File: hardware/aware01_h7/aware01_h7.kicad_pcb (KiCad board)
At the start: 4 copper layers, 76.7 x 110 mm, 138 parts, among them IC2 TLV320AIC3204IRHBR, J1 Conn_01x06_Pin, J10 CV1_IN, J11 InL, J13 OutR, J2 Conn_01x03_Pin, J3 Conn_02x05_Odd_Even, J4 InR, J5 GATE1_IN, J6 OutL, J7 GATE2_IN, J8 CV2_IN, J9 V/OCT_IN, Q1 MMBT3904, Q2 MMBT3904, SW1 SW_Push, SW2 SW_Push, SW3 SW_Push, U1 STM32H7B0ZBTx, U10 NE5532DRG4, U11 LMV722IDR, U13 LMV722IDR, U2 IS45S16800F-7TLA2, U3 10k, U4 10k, U5 10k, U6 10k, U7 LM1117MP-3.3, U8 LM4040DBZ-10, U9 NE5532DRG4, Y1 WE-XTAL 24.0MHz 50ppm

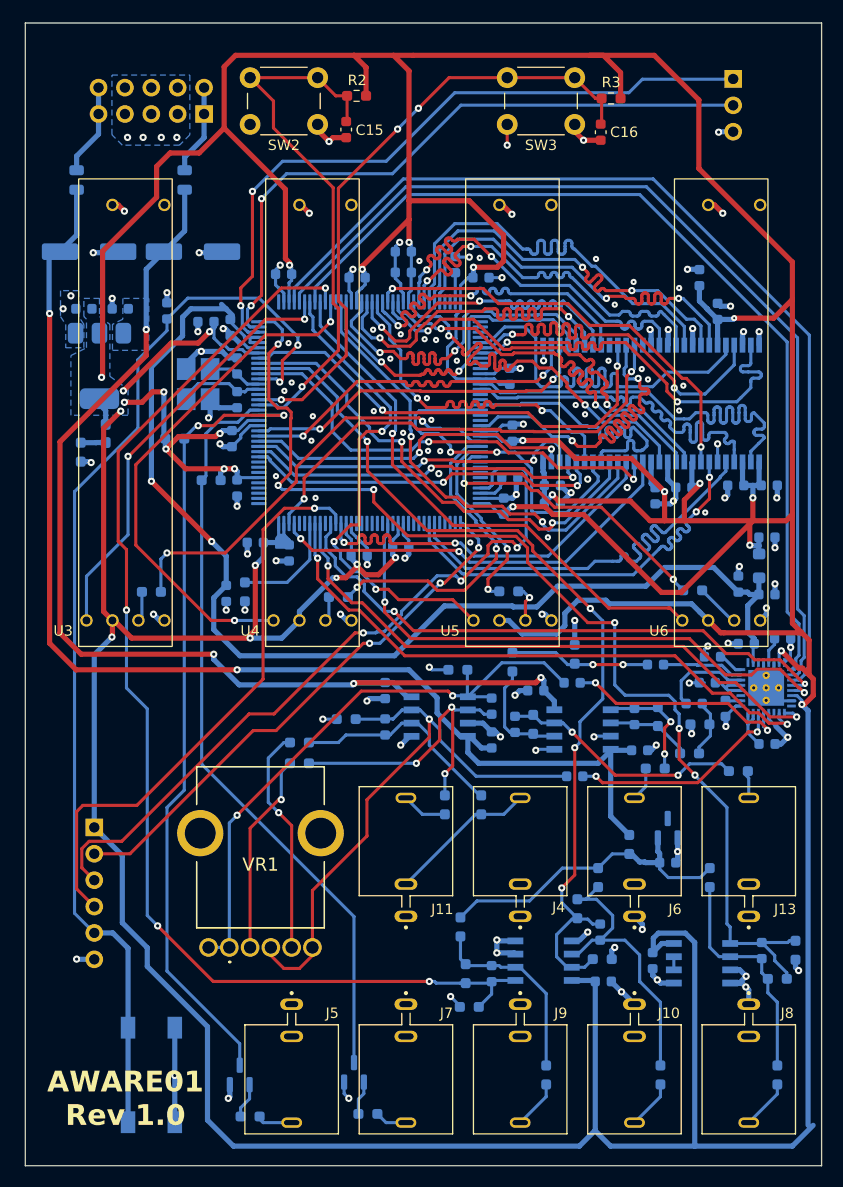
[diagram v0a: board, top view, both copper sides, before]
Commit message: add series termination resistors
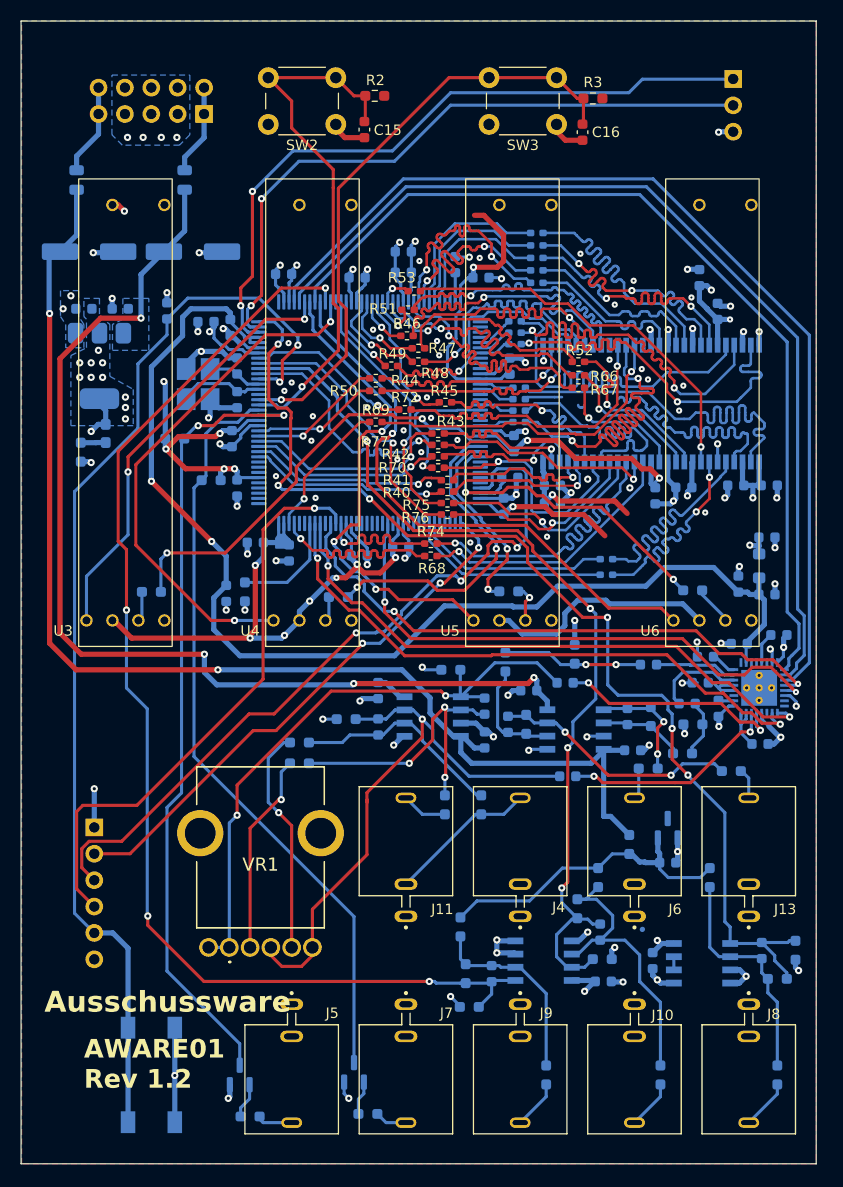
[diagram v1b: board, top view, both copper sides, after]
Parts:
- added R40: 10, Resistor_SMD:R_0402_1005Metric_Pad0.72x0.64mm_HandSolder, F.Cu at (201.5, 80.6)
- added R41: 10, Resistor_SMD:R_0402_1005Metric_Pad0.72x0.64mm_HandSolder, F.Cu at (201.5, 79.5)
- added R42: 10, Resistor_SMD:R_0402_1005Metric_Pad0.72x0.64mm_HandSolder, F.Cu at (200.6, 77.2)
- added R43: 10, Resistor_SMD:R_0402_1005Metric_Pad0.72x0.64mm_HandSolder, F.Cu at (200.6, 75.0)
- added R44: 10, Resistor_SMD:R_0402_1005Metric_Pad0.72x0.64mm_HandSolder, F.Cu at (194.6, 69.7)
- added R45: 10, Resistor_SMD:R_0402_1005Metric_Pad0.72x0.64mm_HandSolder, F.Cu at (201.3, 72.0)
- added R46: 10, Resistor_SMD:R_0402_1005Metric_Pad0.72x0.64mm_HandSolder, F.Cu at (197.6, 65.6)
- added R47: 10, Resistor_SMD:R_0402_1005Metric_Pad0.72x0.64mm_HandSolder, F.Cu at (198.7, 66.8)
- added R48: 10, Resistor_SMD:R_0402_1005Metric_Pad0.72x0.64mm_HandSolder, F.Cu at (198.7, 68.1)
- added R49: 10, Resistor_SMD:R_0402_1005Metric_Pad0.72x0.64mm_HandSolder, F.Cu at (196.1, 68.5)
- added R50: 10, Resistor_SMD:R_0402_1005Metric_Pad0.72x0.64mm_HandSolder, F.Cu at (194.6, 70.9)
- added R51: 10, Resistor_SMD:R_0402_1005Metric_Pad0.72x0.64mm_HandSolder, F.Cu at (197.7, 63.1)
- added R52: 10, Resistor_SMD:R_0402_1005Metric_Pad0.72x0.64mm_HandSolder, F.Cu at (214.1, 68.1)
- added R53: 10, Resistor_SMD:R_0402_1005Metric_Pad0.72x0.64mm_HandSolder, F.Cu at (198.3, 61.3)
- added R54: 10, Resistor_SMD:R_0402_1005Metric_Pad0.72x0.64mm_HandSolder, B.Cu at (216.8, 88.6)
- added R55: 10, Resistor_SMD:R_0402_1005Metric_Pad0.72x0.64mm_HandSolder, B.Cu at (216.8, 87.1)
- added R56: 10, Resistor_SMD:R_0402_1005Metric_Pad0.72x0.64mm_HandSolder, B.Cu at (208.4, 71.7)
- added R57: 10, Resistor_SMD:R_0402_1005Metric_Pad0.72x0.64mm_HandSolder, B.Cu at (208.4, 70.6)
- added R58: 10, Resistor_SMD:R_0402_1005Metric_Pad0.72x0.64mm_HandSolder, B.Cu at (210.1, 60.5)
- added R59: 10, Resistor_SMD:R_0402_1005Metric_Pad0.72x0.64mm_HandSolder, B.Cu at (210.1, 59.3)
- added R60: 10, Resistor_SMD:R_0402_1005Metric_Pad0.72x0.64mm_HandSolder, B.Cu at (210.1, 55.7)
- added R61: 10, Resistor_SMD:R_0402_1005Metric_Pad0.72x0.64mm_HandSolder, B.Cu at (210.1, 56.9)
- added R62: 10, Resistor_SMD:R_0402_1005Metric_Pad0.72x0.64mm_HandSolder, B.Cu at (210.1, 58.1)
- added R63: 10, Resistor_SMD:R_0402_1005Metric_Pad0.72x0.64mm_HandSolder, B.Cu at (208.0, 64.2)
- added R64: 10, Resistor_SMD:R_0402_1005Metric_Pad0.72x0.64mm_HandSolder, B.Cu at (208.0, 65.3)
- added R65: 10, Resistor_SMD:R_0402_1005Metric_Pad0.72x0.64mm_HandSolder, B.Cu at (208.0, 66.4)
- added R66: 10, Resistor_SMD:R_0402_1005Metric_Pad0.72x0.64mm_HandSolder, F.Cu at (214.1, 69.4)
- added R67: 10, Resistor_SMD:R_0402_1005Metric_Pad0.72x0.64mm_HandSolder, F.Cu at (214.1, 70.6)
- added R68: 10, Resistor_SMD:R_0402_1005Metric_Pad0.72x0.64mm_HandSolder, F.Cu at (199.9, 86.8)
- added R69: 10, Resistor_SMD:R_0402_1005Metric_Pad0.72x0.64mm_HandSolder, F.Cu at (194.6, 73.9)
- added R70: 10, Resistor_SMD:R_0402_1005Metric_Pad0.72x0.64mm_HandSolder, F.Cu at (200.6, 78.3)
- added R71: 10, Resistor_SMD:R_0402_1005Metric_Pad0.72x0.64mm_HandSolder, B.Cu at (208.4, 72.8)
- added R72: 10, Resistor_SMD:R_0402_1005Metric_Pad0.72x0.64mm_HandSolder, F.Cu at (197.4, 72.7)
- added R73: 10, Resistor_SMD:R_0402_1005Metric_Pad0.72x0.64mm_HandSolder, B.Cu at (208.4, 73.9)
- added R74: 10, Resistor_SMD:R_0402_1005Metric_Pad0.72x0.64mm_HandSolder, F.Cu at (199.9, 85.6)
- added R75: 10, Resistor_SMD:R_0402_1005Metric_Pad0.72x0.64mm_HandSolder, F.Cu at (201.5, 81.7)
- added R76: 10, Resistor_SMD:R_0402_1005Metric_Pad0.72x0.64mm_HandSolder, F.Cu at (201.5, 82.8)
- added R77: 10, Resistor_SMD:R_0402_1005Metric_Pad0.72x0.64mm_HandSolder, F.Cu at (200.6, 76.1)
- U8: value LM4040DBZ-10 -> LM4040DIM3X-10
- moved C15 1.75 mm to (193.5, 45.8)
- moved C16 1.75 mm to (214.5, 46.0)
- moved R2 1.75 mm to (194.5, 42.5)
- moved R3 1.75 mm to (215.5, 42.8)
- moved SW2 1.75 mm to (190.8, 45.2)
- moved SW3 1.75 mm to (212.0, 45.2)
- moved C27 1.01 mm to (207.9, 76.0)
- moved C29 0.97 mm to (207.5, 68.5)
- moved U6 0.85 mm to (227.0, 93.0)
- moved C39 0.68 mm to (231.6, 104.9)
- moved C40 0.68 mm to (226.3, 96.5)
- moved C41 0.68 mm to (227.6, 101.5)
- moved C42 0.68 mm to (225.8, 99.0)
- moved C43 0.68 mm to (194.8, 99.8)
- moved C44 0.68 mm to (205.1, 104.5)
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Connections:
- U2 pad 10: /FMC_D5 -> Net-(U2-DQ5)
- U2 pad 11: /FMC_D6 -> Net-(U2-DQ6)
- U2 pad 13: /FMC_D7 -> Net-(U2-DQ7)
- U2 pad 15: /FMC_NBL0 -> Net-(U2-DQML)
- U2 pad 16: /FMC_SDNWE -> Net-(U2-~{WE})
- U2 pad 17: /FMC_SDNCAS -> Net-(U2-~{CAS})
- U2 pad 18: /FMC_SDNRAS -> Net-(U2-~{RAS})
- U2 pad 19: /FMC_SDNE0 -> Net-(U2-~{CS})
- U2 pad 2: /FMC_D0 -> Net-(U2-DQ0)
- U2 pad 20: /FMC_BA0 -> Net-(U2-BA0)
- U2 pad 21: /FMC_BA1 -> Net-(U2-BA1)
- U2 pad 22: /FMC_A10 -> Net-(U2-A10)
- U2 pad 23: /FMC_A0 -> Net-(U2-A0)
- U2 pad 24: /FMC_A1 -> Net-(U2-A1)
- U2 pad 25: /FMC_A2 -> Net-(U2-A2)
- U2 pad 26: /FMC_A3 -> Net-(U2-A3)
- U2 pad 29: /FMC_A4 -> Net-(U2-A4)
- U2 pad 30: /FMC_A5 -> Net-(U2-A5)
- U2 pad 31: /FMC_A6 -> Net-(U2-A6)
- U2 pad 32: /FMC_A7 -> Net-(U2-A7)
- U2 pad 33: /FMC_A8 -> Net-(U2-A8)
- U2 pad 34: /FMC_A9 -> Net-(U2-A9)
- U2 pad 35: /FMC_A11 -> Net-(U2-A11)
- U2 pad 37: /FMC_SDCKE0 -> Net-(U2-CKE)
- U2 pad 38: /FMC_SDCLK -> Net-(U2-CLK)
- U2 pad 39: /FMC_NBL1 -> Net-(U2-DQMH)
- U2 pad 4: /FMC_D1 -> Net-(U2-DQ1)
- U2 pad 42: /FMC_D8 -> Net-(U2-DQ8)
- U2 pad 44: /FMC_D9 -> Net-(U2-DQ9)
- U2 pad 45: /FMC_D10 -> Net-(U2-DQ10)
- U2 pad 47: /FMC_D11 -> Net-(U2-DQ11)
- U2 pad 48: /FMC_D12 -> Net-(U2-DQ12)
- U2 pad 5: /FMC_D2 -> Net-(U2-DQ2)
- U2 pad 50: /FMC_D13 -> Net-(U2-DQ13)
- U2 pad 51: /FMC_D14 -> Net-(U2-DQ14)
- U2 pad 53: /FMC_D15 -> Net-(U2-DQ15)
- U2 pad 7: /FMC_D3 -> Net-(U2-DQ3)
- U2 pad 8: /FMC_D4 -> Net-(U2-DQ4)
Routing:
- net +3.3V: track 742.1 -> 246.5 mm, vias 30 -> 42
- net /FMC_D0: track 44.8 -> 3.29 mm
- net /FMC_D13: track 44.8 -> 3.66 mm
- net Net-(U2-CLK): track 0.00 -> 40.3 mm, vias 0 -> 2
- net Net-(U2-DQ13): track 0.00 -> 40.2 mm
- net Net-(U2-DQ0): track 0.00 -> 40.0 mm
- net /FMC_D4: track 42.0 -> 3.08 mm, vias 2 -> 1
- net Net-(U2-DQ4): track 0.00 -> 37.9 mm, vias 0 -> 1
- net Net-(U2-DQ15): track 0.00 -> 37.6 mm, vias 0 -> 2
- net Net-(U2-DQ14): track 0.00 -> 37.0 mm, vias 0 -> 2
- net /FMC_D15: track 39.9 -> 3.09 mm, vias 2 -> 0
- net /FMC_D14: track 40.1 -> 3.34 mm, vias 2 -> 0
- net /FMC_D1: track 37.9 -> 3.53 mm
- net /FMC_SDCLK: track 37.5 -> 3.28 mm, vias 2 -> 0
- net /FMC_NBL1: track 45.8 -> 13.5 mm, vias 2 -> 1
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- added copper zone on F.Cu, net +3.3V
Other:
- board size 76.7 x 110 mm -> 76.6 x 110 mm
- board text added: "AWARE01 Rev 1.2"
- board text added: "Ausschussware"
- board text removed: "AWARE01 Rev 1.0"
